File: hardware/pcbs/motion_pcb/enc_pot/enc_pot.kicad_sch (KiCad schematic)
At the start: 11 parts

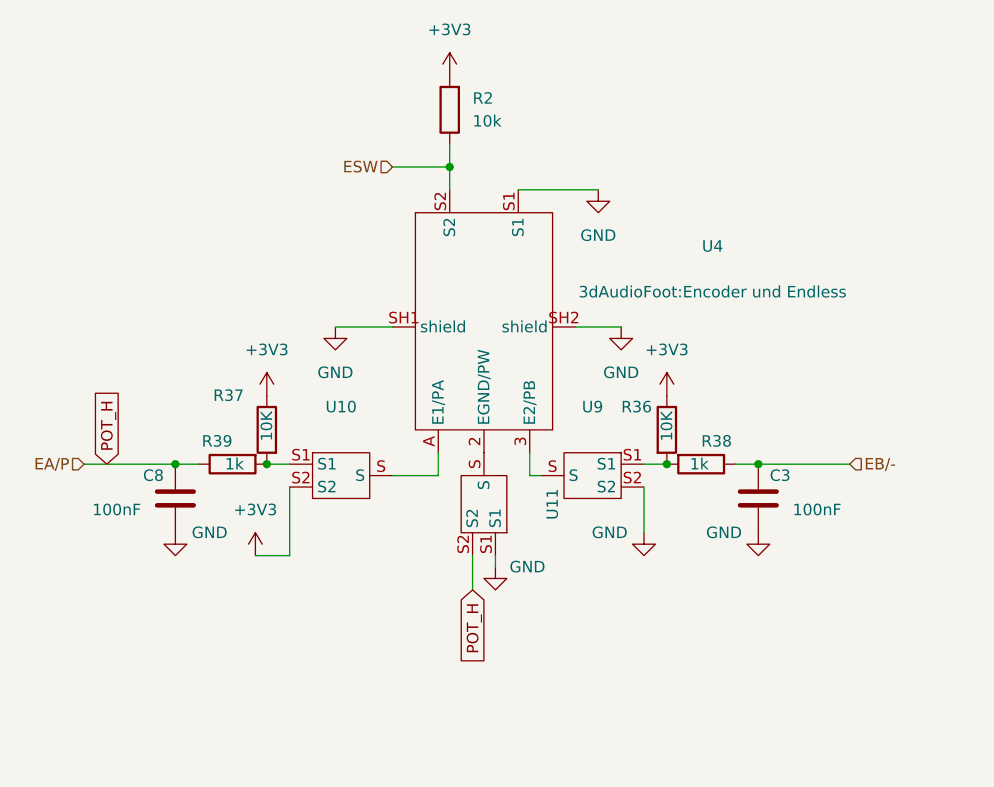
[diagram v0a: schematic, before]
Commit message: created submodule for enc pot mix
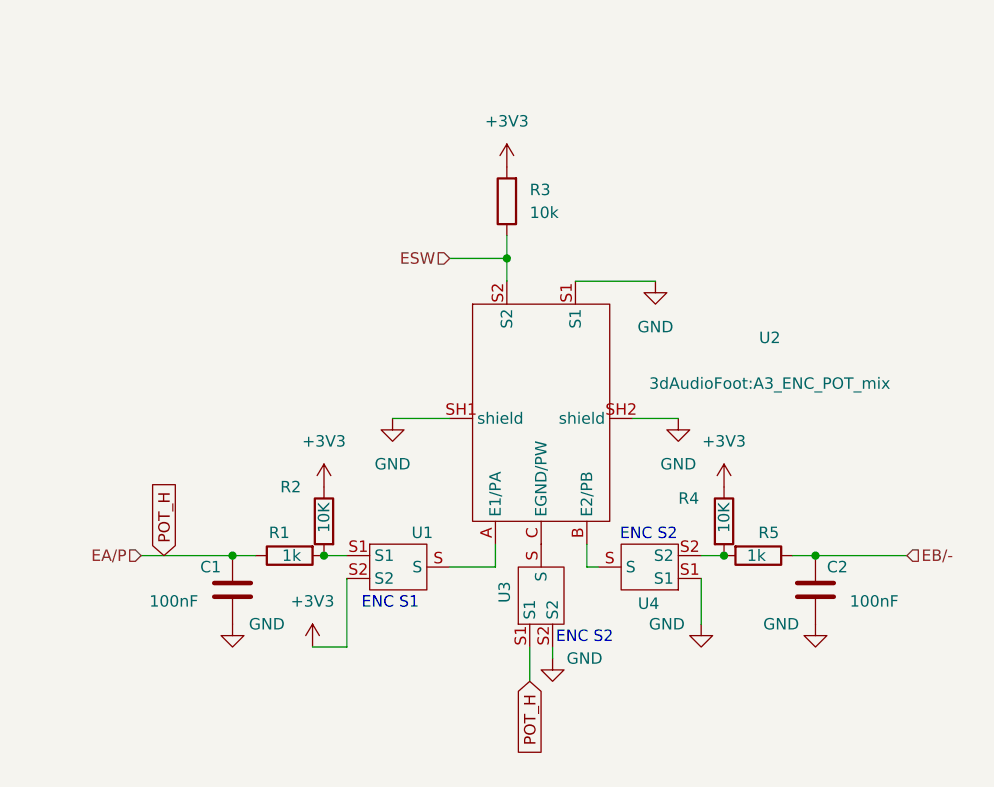
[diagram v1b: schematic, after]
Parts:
- R1: renamed from R39; footprint Resistor_SMD:R_1206_3216Metric -> Resistor_SMD:R_1206_3216Metric_Pad1.30x1.75mm_HandSolder
- R2: renamed from R37; footprint Resistor_SMD:R_1206_3216Metric -> Resistor_SMD:R_1206_3216Metric_Pad1.30x1.75mm_HandSolder
- R3: renamed from R2; footprint (none) -> Resistor_SMD:R_1206_3216Metric_Pad1.30x1.75mm_HandSolder
- R4: renamed from R36; footprint Resistor_SMD:R_1206_3216Metric -> Resistor_SMD:R_1206_3216Metric_Pad1.30x1.75mm_HandSolder
- R5: renamed from R38; footprint Resistor_SMD:R_1206_3216Metric -> Resistor_SMD:R_1206_3216Metric_Pad1.30x1.75mm_HandSolder
- U2: renamed from U4; footprint 3dAudioFoot:Encoder und Endless -> 3dAudioFoot:A3_ENC_POT_mix
- renumbered C8 to C1, C3 to C2, U10 to U1, U11 to U3, U9 to U4
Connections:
- net GND: now also U3.S2, U4.S1; no longer U3.S1, U4.S2
- net POT_H: now also U3.S1; no longer U3.S2
- net at U3.S: now also U2.C (EGND/PW); no longer U2.2 (EGND/PW)
- net at U4.S: now also U2.B (E2/PB); no longer U2.3 (E2/PB)
- net at R4.2, R5.2: now also U4.S2; no longer U4.S1
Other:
- note added: "ENC S1"
- note added: "ENC S2"
- moved on the sheet: C1, C2, R1, R2, R3, R4, R5, U1, U2, U3, U4

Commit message: changing labels
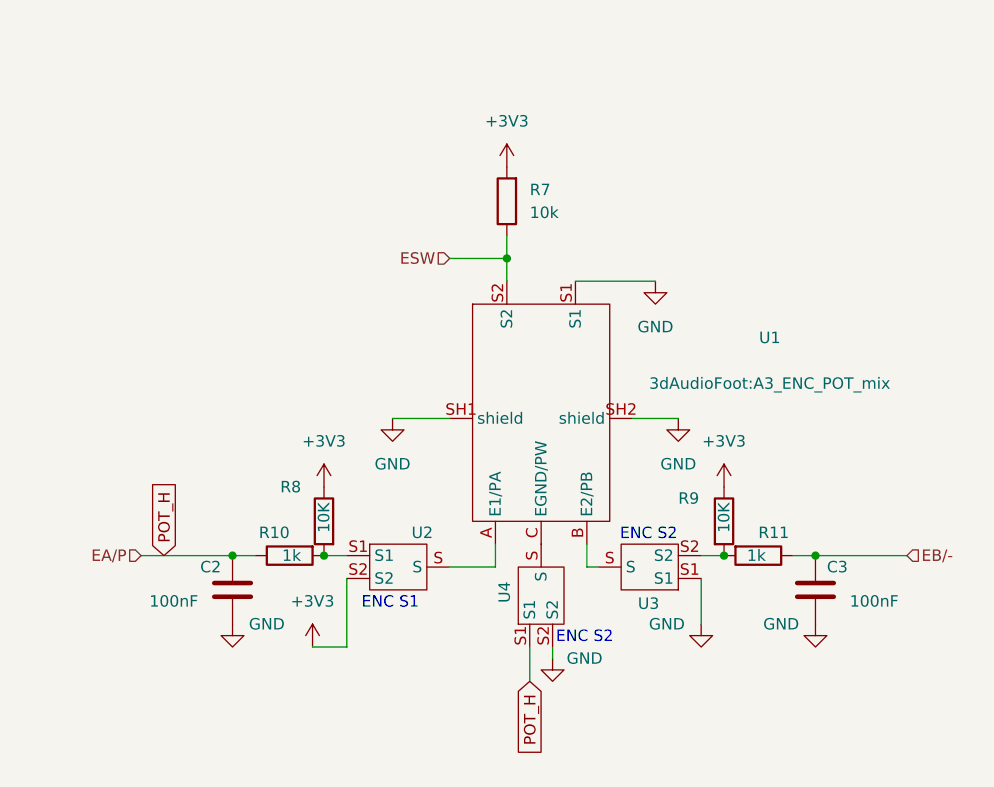
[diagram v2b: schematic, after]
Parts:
- U2: renamed from U1; footprint 3dAudioFoot:A3_1and2 -> 3dAudioFoot:a3_jumper_fix
- U3: renamed from U4; footprint 3dAudioFoot:A3_1and2 -> 3dAudioFoot:a3_jumper_fix
- U4: renamed from U3; footprint 3dAudioFoot:A3_1and2 -> 3dAudioFoot:a3_jumper_fix
- renumbered C1 to C2, C2 to C3, R1 to R10, R5 to R11, R3 to R7, R2 to R8, R4 to R9, U2 to U1

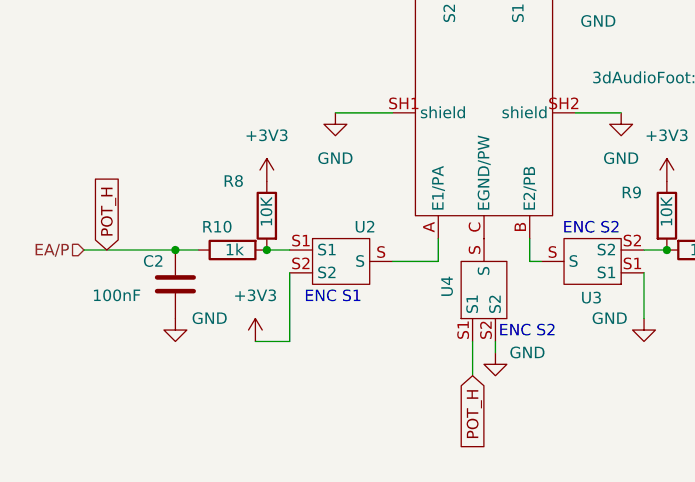
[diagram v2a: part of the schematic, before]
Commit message: finished pcb motion.
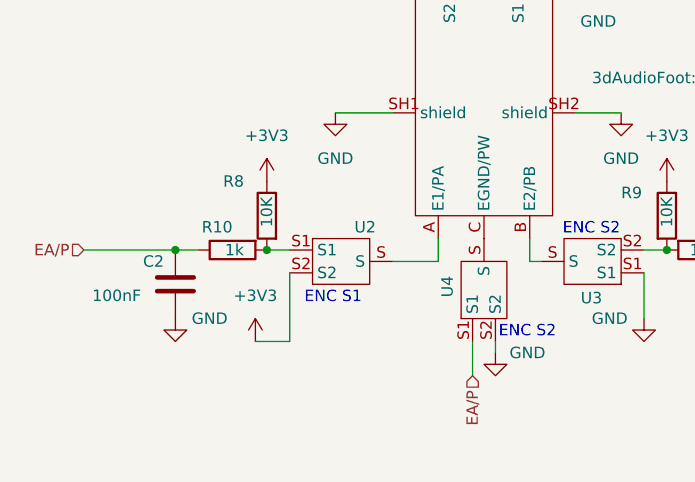
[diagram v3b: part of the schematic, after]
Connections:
- net POT_H renamed EA/P
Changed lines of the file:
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@@
-		)
-	)
-	(global_label "POT_H"
-		(shape input)
-		(at 124.46 100.33 270)
-		(fields_autoplaced yes)
-		(effects
-			(font
-				(size 1.27 1.27)
-			)
-			(justify right)
-		)
-		(property "Intersheetrefs" "${INTERSHEET_REFS}"
-			(at 124.46 109.1814 90)
-			(effects
-				(font
-					(size 1.27 1.27)
-				)
-				(justify right)
-				(hide yes)
-			)
-		)
-	)
-	(global_label "POT_H"
-		(shape input)
-		(at 83.82 86.36 90)
-		(fields_autoplaced yes)
-		(effects
-			(font
-				(size 1.27 1.27)
-			)
-			(justify left)
-		)
-		(property "Intersheetrefs" "${INTERSHEET_REFS}"
-			(at 83.82 77.5086 90)
-			(effects
-				(font
-					(size 1.27 1.27)
-				)
-				(justify left)
-				(hide yes)
-			)
 		)
 	)
@@
 		(shape input)
 		(at 81.28 86.36 180)
+		(effects
+			(font
+				(size 1.27 1.27)
+			)
+			(justify right)
+		)
+	)
+	(hierarchical_label "EA{slash}P"
+		(shape input)
+		(at 124.46 100.33 270)
 		(effects
 			(font
@@
 				)
 			)
+			(project "enc_pot"
+				(path "/4baa2154-55bc-4328-a429-fe83e4ff4690"
+					(reference "#PWR?")
+					(unit 1)
+				)
+			)
 		)
 	)
@@
 				(path "/1501dcbd-05c1-4298-b373-c91a1b0991c0/1fbc53d6-06b1-4900-afa8-0edfe91083f6/c5bb5cd1-3fb8-4e44-89d0-81eebce668db"
 					(reference "U32")
+					(unit 1)
+				)
+			)
+			(project "enc_pot"
+				(path "/4baa2154-55bc-4328-a429-fe83e4ff4690"
+					(reference "U?")
 					(unit 1)
 				)
@@
 				)
 			)
+			(project "enc_pot"
+				(path "/4baa2154-55bc-4328-a429-fe83e4ff4690"
+					(reference "#PWR?")
+					(unit 1)
+				)
+			)
 		)
 	)
@@
 				(path "/1501dcbd-05c1-4298-b373-c91a1b0991c0/1fbc53d6-06b1-4900-afa8-0edfe91083f6/c5bb5cd1-3fb8-4e44-89d0-81eebce668db"
 					(reference "R63")
+					(unit 1)
+				)
+			)
+			(project "enc_pot"
+				(path "/4baa2154-55bc-4328-a429-fe83e4ff4690"
+					(reference "R?")
 					(unit 1)
 				)
@@
 				)
 			)
+			(project "enc_pot"
+				(path "/4baa2154-55bc-4328-a429-fe83e4ff4690"
+					(reference "#PWR?")
+					(unit 1)
+				)
+			)
 		)
 	)
@@
 				)
 			)
+			(project "enc_pot"
+				(path "/4baa2154-55bc-4328-a429-fe83e4ff4690"
+					(reference "C?")
+					(unit 1)
+				)
+			)
 		)
 	)
@@
 				)
 			)
+			(project "enc_pot"
+				(path "/4baa2154-55bc-4328-a429-fe83e4ff4690"
+					(reference "R?")
+					(unit 1)
+				)
+			)
 		)
 	)
@@
 				(path "/1501dcbd-05c1-4298-b373-c91a1b0991c0/1fbc53d6-06b1-4900-afa8-0edfe91083f6/c5bb5cd1-3fb8-4e44-89d0-81eebce668db"
 					(reference "U31")
+					(unit 1)
+				)
+			)
+			(project "enc_pot"
+				(path "/4baa2154-55bc-4328-a429-fe83e4ff4690"
+					(reference "U?")
 					(unit 1)
 				)
@@
 				)
 			)
+			(project "enc_pot"
+				(path "/4baa2154-55bc-4328-a429-fe83e4ff4690"
+					(reference "R?")
+					(unit 1)
+				)
+			)
 		)
 	)
@@
 				)
 			)
+			(project "enc_pot"
+				(path "/4baa2154-55bc-4328-a429-fe83e4ff4690"
+					(reference "#PWR?")
+					(unit 1)
+				)
+			)
 		)
 	)
@@
 				)
 			)
+			(project "enc_pot"
+				(path "/4baa2154-55bc-4328-a429-fe83e4ff4690"
+					(reference "C?")
+					(unit 1)
+				)
+			)
 		)
 	)
@@
 				(path "/1501dcbd-05c1-4298-b373-c91a1b0991c0/1fbc53d6-06b1-4900-afa8-0edfe91083f6/c5bb5cd1-3fb8-4e44-89d0-81eebce668db"
 					(reference "U30")
+					(unit 1)
+				)
+			)
+			(project "enc_pot"
+				(path "/4baa2154-55bc-4328-a429-fe83e4ff4690"
+					(reference "U?")
 					(unit 1)
 				)
@@
 				)
 			)
+			(project "enc_pot"
+				(path "/4baa2154-55bc-4328-a429-fe83e4ff4690"
+					(reference "#PWR?")
+					(unit 1)
+				)
+			)
 		)
 	)
@@
 				(path "/1501dcbd-05c1-4298-b373-c91a1b0991c0/1fbc53d6-06b1-4900-afa8-0edfe91083f6/c5bb5cd1-3fb8-4e44-89d0-81eebce668db"
 					(reference "U29")
+					(unit 1)
+				)
+			)
+			(project "enc_pot"
+				(path "/4baa2154-55bc-4328-a429-fe83e4ff4690"
+					(reference "U?")
 					(unit 1)
 				)
@@
 				)
 			)
+			(project "enc_pot"
+				(path "/4baa2154-55bc-4328-a429-fe83e4ff4690"
+					(reference "#PWR?")
+					(unit 1)
+				)
+			)
 		)
 	)
@@
 				)
 			)
+			(project "enc_pot"
+				(path "/4baa2154-55bc-4328-a429-fe83e4ff4690"
+					(reference "#PWR?")
+					(unit 1)
+				)
+			)
 		)
 	)
@@
 				)
 			)
+			(project "enc_pot"
+				(path "/4baa2154-55bc-4328-a429-fe83e4ff4690"
+					(reference "#PWR?")
+					(unit 1)
+				)
+			)
 		)
 	)
@@
 				(path "/1501dcbd-05c1-4298-b373-c91a1b0991c0/1fbc53d6-06b1-4900-afa8-0edfe91083f6/c5bb5cd1-3fb8-4e44-89d0-81eebce668db"
 					(reference "R67")
+					(unit 1)
+				)
+			)
+			(project "enc_pot"
+				(path "/4baa2154-55bc-4328-a429-fe83e4ff4690"
+					(reference "R?")
 					(unit 1)
 				)
@@
 				)
 			)
+			(project "enc_pot"
+				(path "/4baa2154-55bc-4328-a429-fe83e4ff4690"
+					(reference "#PWR?")
+					(unit 1)
+				)
+			)
 		)
 	)
@@
 				(path "/1501dcbd-05c1-4298-b373-c91a1b0991c0/1fbc53d6-06b1-4900-afa8-0edfe91083f6/c5bb5cd1-3fb8-4e44-89d0-81eebce668db"
 					(reference "R65")
+					(unit 1)
+				)
+			)
+			(project "enc_pot"
+				(path "/4baa2154-55bc-4328-a429-fe83e4ff4690"
+					(reference "R?")
 					(unit 1)
 				)
@@
 				)
 			)
+			(project "enc_pot"
+				(path "/4baa2154-55bc-4328-a429-fe83e4ff4690"
+					(reference "#PWR?")
+					(unit 1)
+				)
+			)
 		)
 	)
@@
 				)
 			)
-		)
-	)
+			(project "enc_pot"
+				(path "/4baa2154-55bc-4328-a429-fe83e4ff4690"
+					(reference "#PWR?")
+					(unit 1)
+				)
+			)
+		)
+	)
+	(sheet_instances
+		(path "/"
+			(page "1")
+		)
+	)
+	(embedded_fonts no)
 )

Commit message: finished design
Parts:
- C2, C3, R10, R11, R7, R8, R9, U2, U3, U4: now not fitted
